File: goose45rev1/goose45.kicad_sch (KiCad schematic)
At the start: 25 parts, among them SW1 Conn_01x02_Female, SW2 SW_Push, U1 STM32F103CBTx, X1 Crystal_GND24

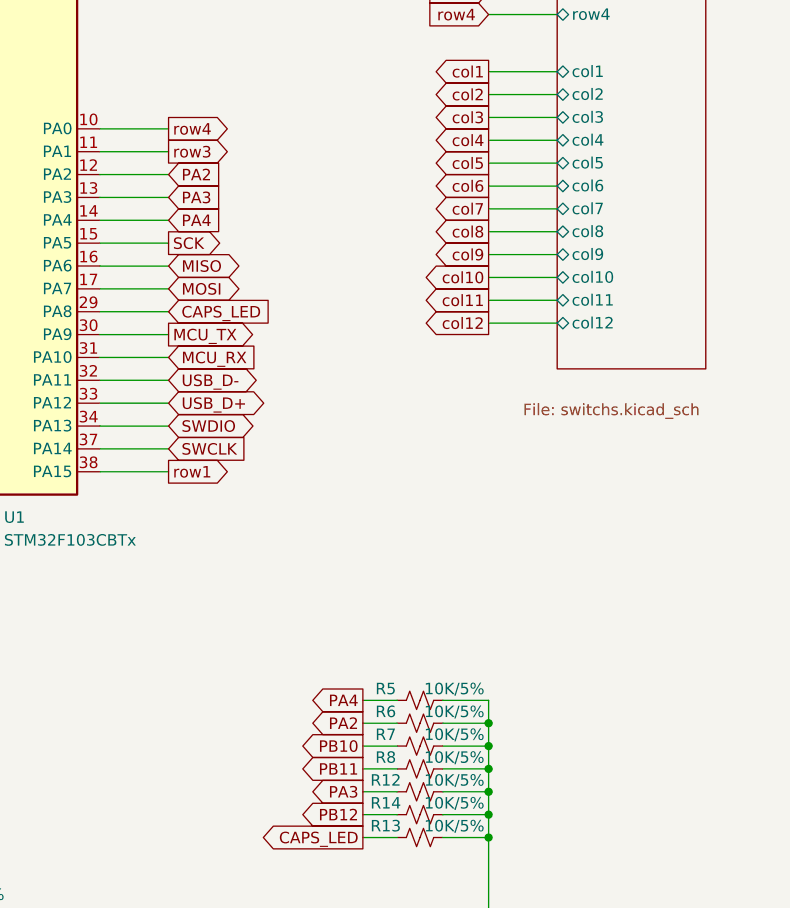
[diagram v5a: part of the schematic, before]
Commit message: update pcb common and update goose45 key loaction
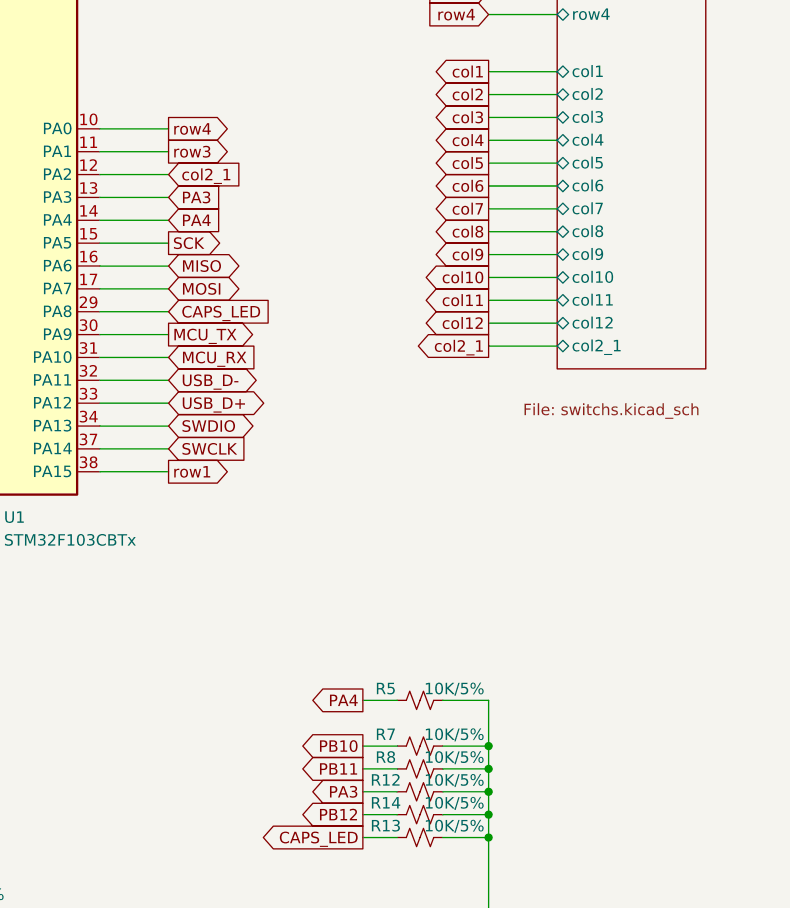
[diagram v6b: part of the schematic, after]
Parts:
- removed R6: 10K/5%, Resistor_SMD:R_0603_1608Metric, symbol Device:R_Small_US
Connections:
- net PA2 renamed col2_1
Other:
- sheet Switchs ports: added col2_1; removed none
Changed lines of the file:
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@@
   (junction (at 43.688 91.948) (diameter 0) (color 0 0 0 0)
   )
-  (junction (at 238.76 132.08) (diameter 0) (color 0 0 0 0)
-  )
   (junction (at 180.34 26.67) (diameter 0) (color 0 0 0 0)
   )
@@
     (stroke (width 0) (type default) (color 0 0 0 0))
   )
-  (wire (pts (xy 233.68 132.08) (xy 238.76 132.08))
-    (stroke (width 0) (type default) (color 0 0 0 0))
-  )
   (wire (pts (xy 151.13 81.28) (xy 162.56 81.28))
     (stroke (width 0) (type default) (color 0 0 0 0))
@@
     (stroke (width 0) (type default) (color 0 0 0 0))
   )
+  (wire (pts (xy 238.76 90.17) (xy 246.38 90.17))
+    (stroke (width 0) (type default) (color 0 0 0 0))
+  )
   (wire (pts (xy 195.58 71.12) (xy 203.2 71.12))
     (stroke (width 0) (type default) (color 0 0 0 0))
@@
     (stroke (width 0) (type default) (color 0 0 0 0))
   )
-  (wire (pts (xy 224.79 132.08) (xy 228.6 132.08))
-    (stroke (width 0) (type default) (color 0 0 0 0))
-  )
   (wire (pts (xy 106.68 154.94) (xy 123.19 154.94))
     (stroke (width 0) (type default) (color 0 0 0 0))
@@
     (stroke (width 0) (type default) (color 0 0 0 0))
   )
-  (wire (pts (xy 238.76 129.54) (xy 238.76 132.08))
+  (wire (pts (xy 238.76 129.54) (xy 238.76 134.62))
     (stroke (width 0) (type default) (color 0 0 0 0))
   )
@@
     (stroke (width 0) (type default) (color 0 0 0 0))
   )
-  (wire (pts (xy 238.76 132.08) (xy 238.76 134.62))
-    (stroke (width 0) (type default) (color 0 0 0 0))
-  )
   (wire (pts (xy 38.608 80.518) (xy 38.608 79.248))
     (stroke (width 0) (type default) (color 0 0 0 0))
@@
     )
   )
+  (global_label "col2_1" (shape output) (at 238.76 90.17 180) (fields_autoplaced)
+    (effects (font (size 1.27 1.27)) (justify right))
+    (property "插入圖紙頁參考" "${INTERSHEET_REFS}" (id 0) (at 230.0574 90.2494 0)
+      (effects (font (size 1.27 1.27)) (justify right) hide)
+    )
+  )
   (global_label "RESET" (shape input) (at 152.4 38.1 180) (fields_autoplaced)
     (effects (font (size 1.27 1.27)) (justify right))
@@
     )
   )
-  (global_label "PA2" (shape output) (at 224.79 132.08 180) (fields_autoplaced)
-    (effects (font (size 1.27 1.27)) (justify right))
-    (property "插入圖紙頁參考" "${INTERSHEET_REFS}" (id 0) (at 218.8088 132.0006 0)
-      (effects (font (size 1.27 1.27)) (justify right) hide)
-    )
-  )
   (global_label "MCU_RX" (shape output) (at 66.04 146.05 0) (fields_autoplaced)
     (effects (font (size 1.27 1.27)) (justify left))
@@
     )
   )
-  (global_label "PA2" (shape input) (at 203.2 71.12 0) (fields_autoplaced)
-    (effects (font (size 1.27 1.27)) (justify left))
-    (property "插入圖紙頁參考" "${INTERSHEET_REFS}" (id 0) (at 209.1812 71.1994 0)
+  (global_label "col2_1" (shape input) (at 203.2 71.12 0) (fields_autoplaced)
+    (effects (font (size 1.27 1.27)) (justify left))
+    (property "插入圖紙頁參考" "${INTERSHEET_REFS}" (id 0) (at 211.9026 71.0406 0)
       (effects (font (size 1.27 1.27)) (justify left) hide)
     )
@@
     (pin "2")
   )
-  (symbol (lib_id "Device:R_Small_US") (at 231.14 132.08 270) (unit 1)
-    (in_bom yes) (on_board yes)
-    (property "Reference" "R6" (id 0) (at 227.33 130.81 90))
-    (property "Value" "10K/5%" (id 1) (at 234.95 130.81 90))
-    (property "Footprint" "Resistor_SMD:R_0603_1608Metric" (id 2) (at 231.14 132.08 0)
-      (effects (font (size 1.27 1.27)) hide)
-    )
-    (property "Datasheet" "~" (id 3) (at 231.14 132.08 0)
-      (effects (font (size 1.27 1.27)) hide)
-    )
-    (pin "1")
-    (pin "2")
-  )
   (symbol (lib_id "Device:C_Small") (at 119.888 46.228 0) (unit 1)
     (in_bom yes) (on_board yes) (fields_autoplaced)
@@
       (effects (font (size 1.27 1.27)) (justify left))
     )
+    (pin "col2_1" bidirectional (at 246.38 90.17 180)
+      (effects (font (size 1.27 1.27)) (justify left))
+    )
   )
   (sheet_instances
@@
       (reference "R5") (unit 1) (value "10K/5%") (footprint "Resistor_SMD:R_0603_1608Metric")
     )
-    (path "/d3ccab6d-5edf-4e3b-be76-16cf06d453b4"
-      (reference "R6") (unit 1) (value "10K/5%") (footprint "Resistor_SMD:R_0603_1608Metric")
-    )
     (path "/2902ec0a-18c3-41a9-bdee-5d52f932a4e4"
       (reference "R7") (unit 1) (value "10K/5%") (footprint "Resistor_SMD:R_0603_1608Metric")
@@
       (reference "SW37") (unit 1) (value "SW_Push") (footprint "Switch_Keyboard_Hotswap_Kailh.pretty:SW_Hotswap_Kailh_MX")
     )
+    (path "/960b1d47-d642-4381-b755-44496f6f685c/64eda88b-5930-468b-a762-75cf5c88a34c"
+      (reference "SW37_1") (unit 1) (value "SW_Push") (footprint "Switch_Keyboard_Hotswap_Kailh.pretty:SW_Hotswap_Kailh_MX")
+    )
     (path "/960b1d47-d642-4381-b755-44496f6f685c/d986926e-6579-4be1-80d9-80ec0867c6db"
       (reference "SW38") (unit 1) (value "SW_Push") (footprint "Switch_Keyboard_Hotswap_Kailh.pretty:SW_Hotswap_Kailh_MX")
     )
+    (path "/960b1d47-d642-4381-b755-44496f6f685c/8b8c3802-0407-4d45-8c95-2983bd6d7aee"
+      (reference "SW38_1") (unit 1) (value "SW_Push") (footprint "Switch_Keyboard_Hotswap_Kailh.pretty:SW_Hotswap_Kailh_MX")
+    )
     (path "/960b1d47-d642-4381-b755-44496f6f685c/429c3a66-f47a-4a65-9a94-49e9dc8cdffe"
